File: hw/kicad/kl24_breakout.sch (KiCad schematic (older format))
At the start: 65 parts, among them J1 USB-micro-ab, J2 ARM_10PIN, P1 BATT+, P10 TST, P11 TST, P12 TST, P13 TST, P14 TST, P15 TST, P16 TST, P17 TST, P18 TST, P19 TST, P2 BATT-, P20 TST, P21 TST, P22 TST, P23 TST, P24 TST, P25 TST, P26 TST, P27 TST, P28 TST, P29 TST, P3 TST, P30 TST, P31 TST, P32 TST, P33 TST, P34 TST, P35 BATT_BACKUP+, P36 BATT_BACKUP-, P37 USB_V, P38 USB_GND, P4 TST, P5 TST, P6 TST, P7 TST, P8 TST, P9 TST, U1 MCP73831, U2 M25P05-A, U3 MKL24Z64VFM4, U4 MCP1640_SOT23, U5 LP3985, X1 CRYSTAL

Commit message: - remove lv pwr supply
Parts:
- removed C5: 4.7uF, symbol C
- removed C8: 10uF, symbol C
- removed L1: INDUCTOR, symbol INDUCTOR
- removed P35: BATT_BACKUP+, symbol TST
- removed P36: BATT_BACKUP-, symbol TST
- removed R5: 0R, ~, symbol R
- removed R6: 562K, symbol R
- removed R7: 976K, symbol R
- removed U4: MCP1640_SOT23, symbol MCP1640_SOT23
- renumbered C6 to C4, C9 to C5, C4 to C6, P8 to P10, P9 to P11, P10 to P12, P11 to P13, P12 to P14, P13 to P15, P14 to P16, P15 to P17, P16 to P18, P17 to P19, P18 to P20, P19 to P21, P20 to P22, P21 to P23, P22 to P24, P23 to P25, P24 to P26, P25 to P27, P26 to P28, P27 to P29, P37 to P3, P28 to P30, P29 to P31, P30 to P32, P31 to P33, P32 to P34, P33 to P35, P34 to P36, P38 to P4, P3 to P5, P4 to P6, P5 to P7, P6 to P8, P7 to P9, U5 to U4
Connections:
- net labels removed: LV_SUPP_VIN, LV_SUPP_VOUT
- wire segments 152 -> 135
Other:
- note removed: "LV POWER SUPPLY 0.9V-1.7V"
- moved on the sheet: C1, C2, C4, C5, C6, C7, D1, P1, P10, P11, P12, P13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

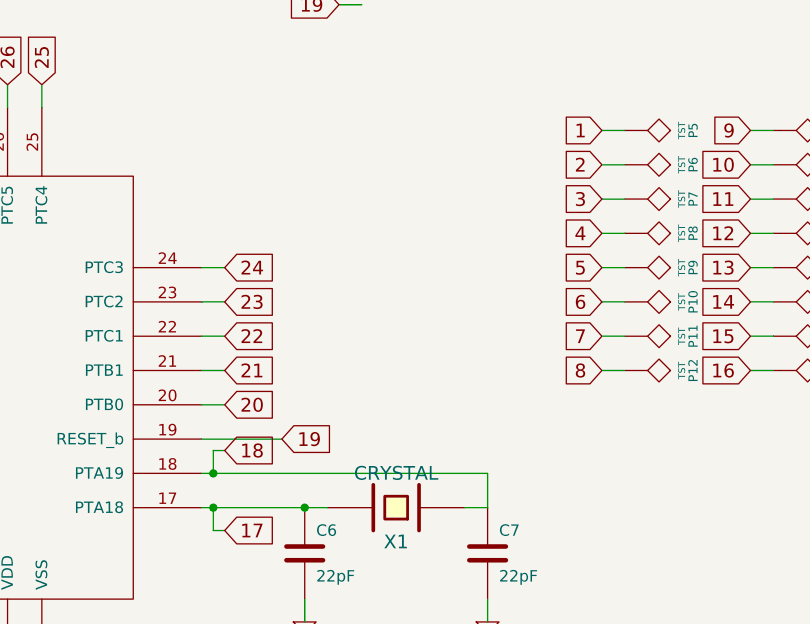
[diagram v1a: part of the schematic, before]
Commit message: - add indicator led to schematic
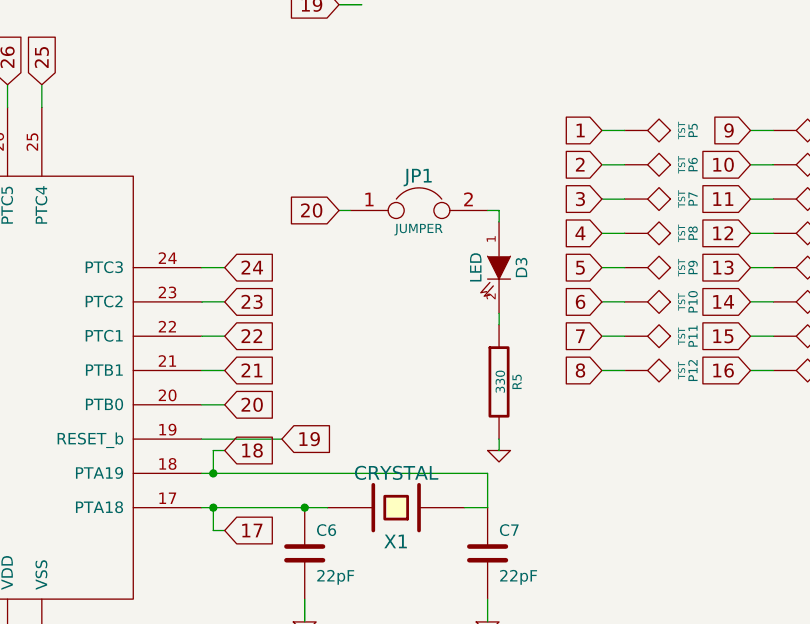
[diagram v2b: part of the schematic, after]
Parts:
- added D3: LED, ~, symbol LED
- added JP1: JUMPER, ~, symbol JUMPER
- added R5: 330, ~, symbol R
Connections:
- wire segments 135 -> 140
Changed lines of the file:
@@
-EESchema Schematic File Version 2  date 5/19/2013 11:25:39 AM
+EESchema Schematic File Version 2  date 5/24/2013 8:28:12 AM
 LIBS:power
 LIBS:device
@@
 Sheet 1 1
 Title ""
-Date "19 may 2013"
+Date "24 may 2013"
 Rev ""
 Comp ""
@@
 Text Notes 2100 1350 0    60   ~ 0
 USB VPWR TST POINTS
+Text GLabel 7650 3300 0    60   Input ~ 0
+20
+$Comp
+L JUMPER JP1
+U 1 1 519F5D90
+P 8000 3300
+F 0 "JP1" H 8000 3450 60  0000 C CNN
+F 1 "JUMPER" H 8000 3220 40  0000 C CNN
+F 2 "~" H 8000 3300 60  0000 C CNN
+F 3 "~" H 8000 3300 60  0000 C CNN
+	1    8000 3300
+	1    0    0    -1
+$EndComp
+$Comp
+L LED D3
+U 1 1 519F5D9F
+P 8350 3550
+F 0 "D3" H 8350 3650 50  0000 C CNN
+F 1 "LED" H 8350 3450 50  0000 C CNN
+F 2 "~" H 8350 3550 60  0000 C CNN
+F 3 "~" H 8350 3550 60  0000 C CNN
+	1    8350 3550
+	0    1    1    0
+$EndComp
+$Comp
+L R R5
+U 1 1 519F5DAE
+P 8350 4050
+F 0 "R5" V 8430 4050 40  0000 C CNN
+F 1 "330" V 8357 4051 40  0000 C CNN
+F 2 "~" V 8280 4050 30  0000 C CNN
+F 3 "~" H 8350 4050 30  0000 C CNN
+	1    8350 4050
+	1    0    0    -1
+$EndComp
+$Comp
+L GND #PWR016
+U 1 1 519F5DBB
+P 8350 4350
+F 0 "#PWR016" H 8350 4350 30  0001 C CNN
+F 1 "GND" H 8350 4280 30  0001 C CNN
+F 2 "" H 8350 4350 60  0001 C CNN
+F 3 "" H 8350 4350 60  0001 C CNN
+	1    8350 4350
+	1    0    0    -1
+$EndComp
+Wire Wire Line
+	8350 4350 8350 4300
+Wire Wire Line
+	8350 3800 8350 3750
+Wire Wire Line
+	7650 3300 7700 3300
+Wire Wire Line
+	8300 3300 8350 3300
+Wire Wire Line
+	8350 3300 8350 3350
 $EndSCHEMATC

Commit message: - remove lipo charger
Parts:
- removed C1, C2: 4.7uF, symbol C
- removed D1: LED, symbol LED
- removed D2: DIODESCH, ~, symbol DIODESCH
- removed P1: BATT+, symbol TST
- removed P2: BATT-, symbol TST
- removed R1: 470R, symbol R
- removed R2: 2K, symbol R
- removed U1: MCP73831, symbol MCP73831
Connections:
- net labels removed: LIPO+
- wire segments 140 -> 125
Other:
- note removed: "LIPO CHARGER"
- moved on the sheet: C3, C4, C5, J1, P3, P4, U4

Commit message: remove spi flash (maybe sdio instead)
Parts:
- removed C3: 1uF, symbol C
- removed U2: M25P05-A, symbol M25P05-A
- renumbered C4 to C1, C5 to C2, C6 to C3, C7 to C4, D3 to D1, P3 to P1, P12 to P10, P13 to P11, P14 to P12, P15 to P13, P16 to P14, P17 to P15, P18 to P16, P19 to P17, P20 to P18, P21 to P19, P4 to P2, P22 to P20, P23 to P21, P24 to P22, P25 to P23, P26 to P24, P27 to P25, P28 to P26, P29 to P27, P30 to P28, P31 to P29, P5 to P3, P32 to P30, P33 to P31, P34 to P32, P35 to P33, P36 to P34, P6 to P4, P7 to P5, P8 to P6, P9 to P7, P10 to P8, P11 to P9, R3 to R1, R4 to R2, R5 to R3, U4 to U1, U3 to U2
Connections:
- wire segments 125 -> 116
- no-connect marks 8 -> 6
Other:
- note removed: "SPI FLASH"

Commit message: remove 10 pin header
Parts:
- removed J2: ARM_10PIN, symbol ARM_10PIN
- added JP?: JUMPER, ~, symbol JUMPER
- added P?: SWDIO, symbol TST
- added P?: SWD_VCC, symbol TST
- added P?: SWCLK, symbol TST
- added P?: SWD_GND, symbol TST
- added P?: NRESET, symbol TST
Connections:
- wire segments 116 -> 118
- no-connect marks 6 -> 1
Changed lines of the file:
@@
-EESchema Schematic File Version 2  date 10/5/2013 3:10:17 PM
+EESchema Schematic File Version 2  date 10/11/2013 6:25:26 PM
 LIBS:power
 LIBS:device
@@
 Sheet 1 1
 Title ""
-Date "5 oct 2013"
+Date "11 oct 2013"
 Rev ""
 Comp ""
@@
 $EndDescr
 Wire Wire Line
-	7650 1050 7800 1050
-Wire Wire Line
 	2000 6000 2000 6300
 Wire Wire Line
@@
 Wire Wire Line
 	2000 6300 2100 6300
-Connection ~ 7700 1650
-Wire Wire Line
-	7800 1350 7700 1350
-Wire Wire Line
-	7700 1350 7700 2250
-Wire Wire Line
-	7800 1650 7700 1650
-Wire Wire Line
-	7700 2250 7800 2250
-Wire Wire Line
-	7650 2400 7750 2400
-Wire Wire Line
-	7750 1200 7650 1200
-Wire Wire Line
-	7650 1500 7750 1500
 Wire Wire Line
 	6350 2750 6350 2850
@@
 Wire Wire Line
 	1950 3050 1850 3050
-Text GLabel 7650 1050 0    60   Input ~ 0
+Text GLabel 5400 1550 3    60   Input ~ 0
 3.3V_SUPPLY
-Text GLabel 2200 3500 2    60   Input ~ 0
+Text GLabel 2800 3900 2    60   Input ~ 0
 USB_ID
 Text GLabel 1950 3350 2    60   Input ~ 0
@@
 	1    2700 6150
 	1    0    0    -1
-$EndComp
-$Comp
-L ARM_10PIN J2
-U 1 1 51353F09
-P 8250 1550
-F 0 "J2" H 8250 550 60  0000 C CNN
-F 1 "ARM_10PIN" H 8250 2200 60  0000 C CNN
-F 2 "" H 8250 1550 60  0001 C CNN
-F 3 "" H 8250 1550 60  0001 C CNN
-	1    8250 1550
-	-1   0    0    -1
 $EndComp
 $Comp
@@
 Text Notes 2250 6650 0    60   ~ 0
 3.3V POWER SUPPLY
-Text GLabel 7650 1500 0    60   Input ~ 0
+Text GLabel 5900 1550 3    60   Input ~ 0
 10
-Text GLabel 7650 1200 0    60   Input ~ 0
+Text GLabel 5650 1550 3    60   Input ~ 0
 13
-Text GLabel 7650 2400 0    60   Input ~ 0
+Text GLabel 6150 1550 3    60   Input ~ 0
 19
 $Comp
 L GND #PWR04
 U 1 1 513F9714
-P 7700 2250
-F 0 "#PWR04" H 7700 2250 30  0001 C CNN
-F 1 "GND" H 7700 2180 30  0001 C CNN
-F 2 "" H 7700 2250 60  0001 C CNN
-F 3 "" H 7700 2250 60  0001 C CNN
-	1    7700 2250
+P 6400 1550
+F 0 "#PWR04" H 6400 1550 30  0001 C CNN
+F 1 "GND" H 6400 1480 30  0001 C CNN
+F 2 "" H 6400 1550 60  0001 C CNN
+F 3 "" H 6400 1550 60  0001 C CNN
+	1    6400 1550
 	1    0    0    -1
 $EndComp
@@
 	-1   0    0    1
 $EndComp
-NoConn ~ 7750 1800
-NoConn ~ 7800 1950
-NoConn ~ 7750 2100
 NoConn ~ 3350 6300
 $Comp
@@
 Text Notes 800  4200 0    60   ~ 0
 id pin- gnd for host, float for device
-NoConn ~ 1850 3500
-NoConn ~ 2200 3500
 $Comp
 L TST P1
@@
 Wire Wire Line
 	1850 5850 1850 6000
+Text GLabel 2800 4100 2    60   Input ~ 0
+20
+Wire Wire Line
+	2800 3900 2800 4100
+$Comp
+L JUMPER JP?
+U 1 1 52587B78
+P 2450 3600
+F 0 "JP?" H 2450 3750 60  0000 C CNN
+F 1 "JUMPER" H 2450 3520 40  0000 C CNN
+F 2 "~" H 2450 3600 60  0000 C CNN
+F 3 "~" H 2450 3600 60  0000 C CNN
+	1    2450 3600
+	1    0    0    -1
+$EndComp
+Wire Wire Line
+	1850 3500 2150 3500
+Wire Wire Line
+	2150 3500 2150 3600
+Wire Wire Line
+	2750 3600 2750 4000
+Wire Wire Line
+	2750 4000 2800 4000
+Connection ~ 2800 4000
+$Comp
+L TST P?
+U 1 1 52587D3C
+P 5650 1400
+F 0 "P?" H 5650 1700 40  0000 C CNN
+F 1 "SWDIO" H 5650 1650 30  0000 C CNN
+F 2 "" H 5650 1400 60  0001 C CNN
+F 3 "" H 5650 1400 60  0001 C CNN
+	1    5650 1400
+	1    0    0    -1
+$EndComp
+$Comp
+L TST P?
+U 1 1 52587D47
+P 5400 1400
+F 0 "P?" H 5400 1700 40  0000 C CNN
+F 1 "SWD_VCC" H 5400 1650 30  0000 C CNN
+F 2 "" H 5400 1400 60  0001 C CNN
+F 3 "" H 5400 1400 60  0001 C CNN
+	1    5400 1400
+	1    0    0    -1
+$EndComp
+$Comp
+L TST P?
+U 1 1 52587D52
+P 5900 1400
+F 0 "P?" H 5900 1700 40  0000 C CNN
+F 1 "SWCLK" H 5900 1650 30  0000 C CNN
+F 2 "" H 5900 1400 60  0001 C CNN
+F 3 "" H 5900 1400 60  0001 C CNN
+	1    5900 1400
+	1    0    0    -1
+$EndComp
+$Comp
+L TST P?
+U 1 1 52587D67
+P 6400 1400
+F 0 "P?" H 6400 1700 40  0000 C CNN
+F 1 "SWD_GND" H 6400 1650 30  0000 C CNN
+F 2 "" H 6400 1400 60  0001 C CNN
+F 3 "" H 6400 1400 60  0001 C CNN
+	1    6400 1400
+	1    0    0    -1
+$EndComp
+$Comp
+L TST P?
+U 1 1 52587D72
+P 6150 1400
+F 0 "P?" H 6150 1700 40  0000 C CNN
+F 1 "NRESET" H 6150 1650 30  0000 C CNN
+F 2 "" H 6150 1400 60  0001 C CNN
+F 3 "" H 6150 1400 60  0001 C CNN
+	1    6150 1400
+	1    0    0    -1
+$EndComp
+Wire Wire Line
+	5400 1400 5400 1550
+Wire Wire Line
+	5650 1550 5650 1400
+Wire Wire Line
+	5900 1400 5900 1550
+Wire Wire Line
+	6150 1550 6150 1400
+Wire Wire Line
+	6400 1400 6400 1550
 $EndSCHEMATC

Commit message: fix up a bit
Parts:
- removed JP?: JUMPER, ~, symbol JUMPER
- added R3: 330, ~, symbol R
- gave numbers to parts that had none: 5
- renumbered C3 to C1, C4 to C2, C1 to C3, C2 to C4, P3 to P1, P12 to P10, P13 to P11, P14 to P12, P15 to P13, P16 to P14, P17 to P15, P18 to P16, P19 to P17, P20 to P18, P21 to P19, P4 to P2, P22 to P20, P23 to P21, P24 to P22, P25 to P23, P26 to P24, P27 to P25, P28 to P26, P29 to P27, P30 to P28, P31 to P29, P5 to P3, P32 to P30, P33 to P31, P34 to P32, P1 to P33, P2 to P34, P6 to P4, P7 to P5, P8 to P6, P9 to P7, P10 to P8, P11 to P9, R3 to R4, U2 to U1, U1 to U2
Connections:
- net 20: now also R3.2
- net at J1.4 (ID): now also R3.1
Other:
- note added: "no pop"
- moved on the sheet: C1, C2, C3, C4, D1, J1, JP1, P1, P10, P11, P12, P13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

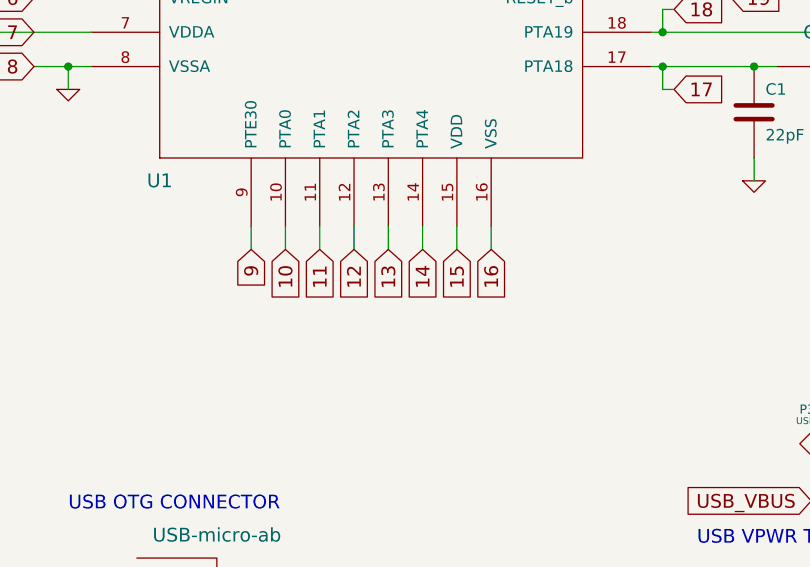
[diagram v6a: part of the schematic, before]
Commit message: all footprints placed, start wiring
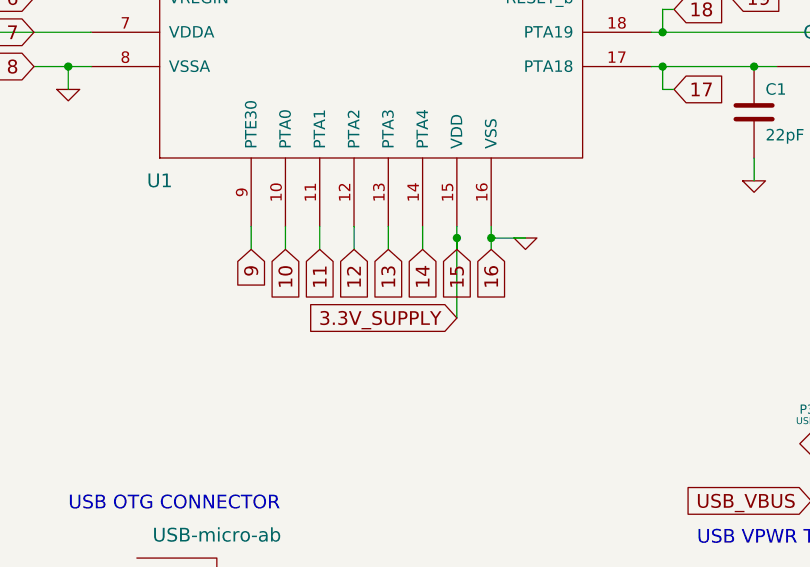
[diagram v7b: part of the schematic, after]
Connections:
- net 16 is gone; now on net GND: P16.1, U1.16 (VSS)
- net 3.3V_SUPPLY is gone; now on net 15: C4.1, P35.1, P7.1, U1.7 (VDDA), U2.5 (VOUT)
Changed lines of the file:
@@
 LIBS:kicadlib
 LIBS:kl24_breakout-cache
-EELAYER 24 0
+EELAYER 27 0
 EELAYER END
 $Descr A4 11693 8268
@@
 Sheet 1 1
 Title ""
-Date "11 oct 2013"
+Date "13 oct 2013"
 Rev ""
 Comp ""
@@
 USB_VBUS
 $Comp
-L GND #PWR3
+L GND #PWR01
 U 1 1 513B6B06
 P 5050 6600
-F 0 "#PWR3" H 5050 6600 30  0001 C CNN
+F 0 "#PWR01" H 5050 6600 30  0001 C CNN
 F 1 "GND" H 5050 6530 30  0001 C CNN
 F 2 "" H 5050 6600 60  0001 C CNN
@@
 $EndComp
 $Comp
-L GND #PWR4
+L GND #PWR02
 U 1 1 513BAD17
 P 7000 3950
-F 0 "#PWR4" H 7000 3950 30  0001 C CNN
+F 0 "#PWR02" H 7000 3950 30  0001 C CNN
 F 1 "GND" H 7000 3880 30  0001 C CNN
 F 2 "" H 7000 3950 60  0001 C CNN
@@
 $EndComp
 $Comp
-L GND #PWR6
+L GND #PWR03
 U 1 1 513BAD27
 P 7800 3950
-F 0 "#PWR6" H 7800 3950 30  0001 C CNN
+F 0 "#PWR03" H 7800 3950 30  0001 C CNN
 F 1 "GND" H 7800 3880 30  0001 C CNN
 F 2 "" H 7800 3950 60  0001 C CNN
@@
 19
 $Comp
-L GND #PWR10
+L GND #PWR04
 U 1 1 513F9714
 P 10600 5750
-F 0 "#PWR10" H 10600 5750 30  0001 C CNN
+F 0 "#PWR04" H 10600 5750 30  0001 C CNN
 F 1 "GND" H 10600 5680 30  0001 C CNN
 F 2 "" H 10600 5750 60  0001 C CNN
@@
 $EndComp
 $Comp
-L GND #PWR8
+L GND #PWR05
 U 1 1 513F9B6C
 P 8250 1400
-F 0 "#PWR8" H 8250 1400 30  0001 C CNN
+F 0 "#PWR05" H 8250 1400 30  0001 C CNN
 F 1 "GND" H 8250 1330 30  0001 C CNN
 F 2 "" H 8250 1400 60  0001 C CNN
@@
 $EndComp
 $Comp
-L GND #PWR9
+L GND #PWR06
 U 1 1 513F9C7F
 P 10000 1350
-F 0 "#PWR9" H 10000 1350 30  0001 C CNN
+F 0 "#PWR06" H 10000 1350 30  0001 C CNN
 F 1 "GND" H 10000 1280 30  0001 C CNN
 F 2 "" H 10000 1350 60  0001 C CNN
@@
 3.3V_SUPPLY
 $Comp
-L GND #PWR2
+L GND #PWR07
 U 1 1 513FA04E
 P 4000 3550
-F 0 "#PWR2" H 4000 3550 30  0001 C CNN
+F 0 "#PWR07" H 4000 3550 30  0001 C CNN
 F 1 "GND" H 4000 3480 30  0001 C CNN
 F 2 "" H 4000 3550 60  0001 C CNN
@@
 $EndComp
 $Comp
-L GND #PWR1
+L GND #PWR08
 U 1 1 513FA1BA
 P 4000 2300
-F 0 "#PWR1" H 4000 2300 30  0001 C CNN
+F 0 "#PWR08" H 4000 2300 30  0001 C CNN
 F 1 "GND" H 4000 2230 30  0001 C CNN
 F 2 "" H 4000 2300 60  0001 C CNN
@@
 	7250 5350 7250 5250
 $Comp
-L GND #PWR5
+L GND #PWR09
 U 1 1 5169787E
 P 7500 5350
-F 0 "#PWR5" H 7500 5350 30  0001 C CNN
+F 0 "#PWR09" H 7500 5350 30  0001 C CNN
 F 1 "GND" H 7500 5280 30  0001 C CNN
 F 2 "" H 7500 5350 60  0001 C CNN
@@
 $EndComp
 $Comp
-L GND #PWR7
+L GND #PWR010
 U 1 1 519F5DBB
 P 7850 3200
-F 0 "#PWR7" H 7850 3200 30  0001 C CNN
+F 0 "#PWR010" H 7850 3200 30  0001 C CNN
 F 1 "GND" H 7850 3130 30  0001 C CNN
 F 2 "" H 7850 3200 60  0001 C CNN
@@
 Text Notes 5700 6150 0    60   ~ 0
 no pop
+$Comp
+L GND #PWR011
+U 1 1 525B1F5C
+P 6000 4200
+F 0 "#PWR011" H 6000 4200 30  0001 C CNN
+F 1 "GND" H 6000 4130 30  0001 C CNN
+F 2 "" H 6000 4200 60  0001 C CNN
+F 3 "" H 6000 4200 60  0001 C CNN
+	1    6000 4200
+	1    0    0    -1
+$EndComp
+Wire Wire Line
+	5850 4200 6000 4200
+Connection ~ 5850 4200
+Text GLabel 5700 4550 0    60   Input ~ 0
+3.3V_SUPPLY
+Wire Wire Line
+	5700 4200 5700 4550
+Connection ~ 5700 4200
 $EndSCHEMATC
